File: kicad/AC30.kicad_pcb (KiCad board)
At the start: 2 copper layers, 173.5 x 122 mm, 119 parts, among them IC1 4013, IC10 555, IC11 4001, IC12 1489, IC13 4070, IC14 4053, IC15 1488, IC2 4001, IC3 4070, IC4 4558, IC5 4013, IC6 4053, IC7 4049, IC8 4013, IC9 4023, J1 Front panel harness 1, J12 Power input, J2 Front panel harness 2, J3 Computer interface (COMP), J4 Control interface, J5 Terminal interface (TERM), Q1 2N5210, Q10 2N5087, Q11 2N5087, Q2 2N5210, Q3 2N5087, Q4 2N5210, Q5 2N5210, Q6 2N5210, Q7 2N5210, Q8 2N5210, Q9 2N5087

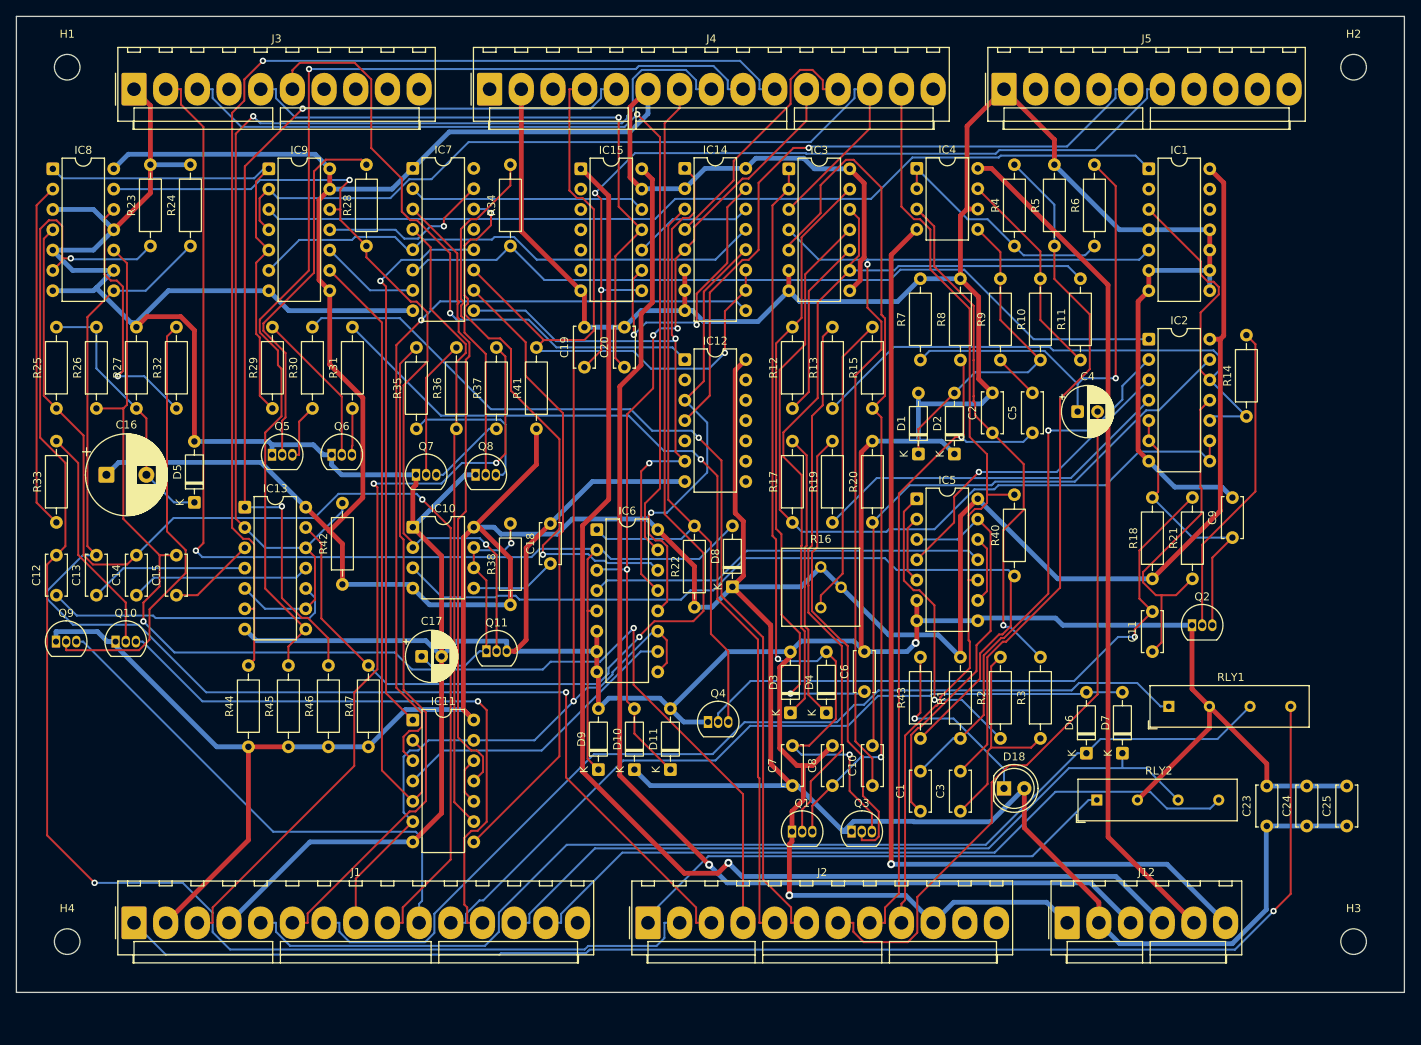
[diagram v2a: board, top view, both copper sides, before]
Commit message: Through-hole board: front-panel jumper pads in place of J1/J2
Both boards now wire the front panel to five rows of 0.1 in through-hole
pads with net names on the silkscreen (J1 SWITCHES, J2 LEDS, J13 MOTOR,
J14 MIC, J15 EAR) instead of the artwork's J1/J2 KK-396 headers.

The through-hole build weights board height at 60 (AC30_HEIGHT_W) so the
bottom row doesn't stretch the board; it is now 173.0 x 126.5 mm, fully
routed, ERC/DRC/parity clean. SMT board unchanged apart from symbol IDs
and the schematic note. AC30-settings.md updated.

Co-Authored-By: Claude Opus 5.5 <noreply@anthropic.com>
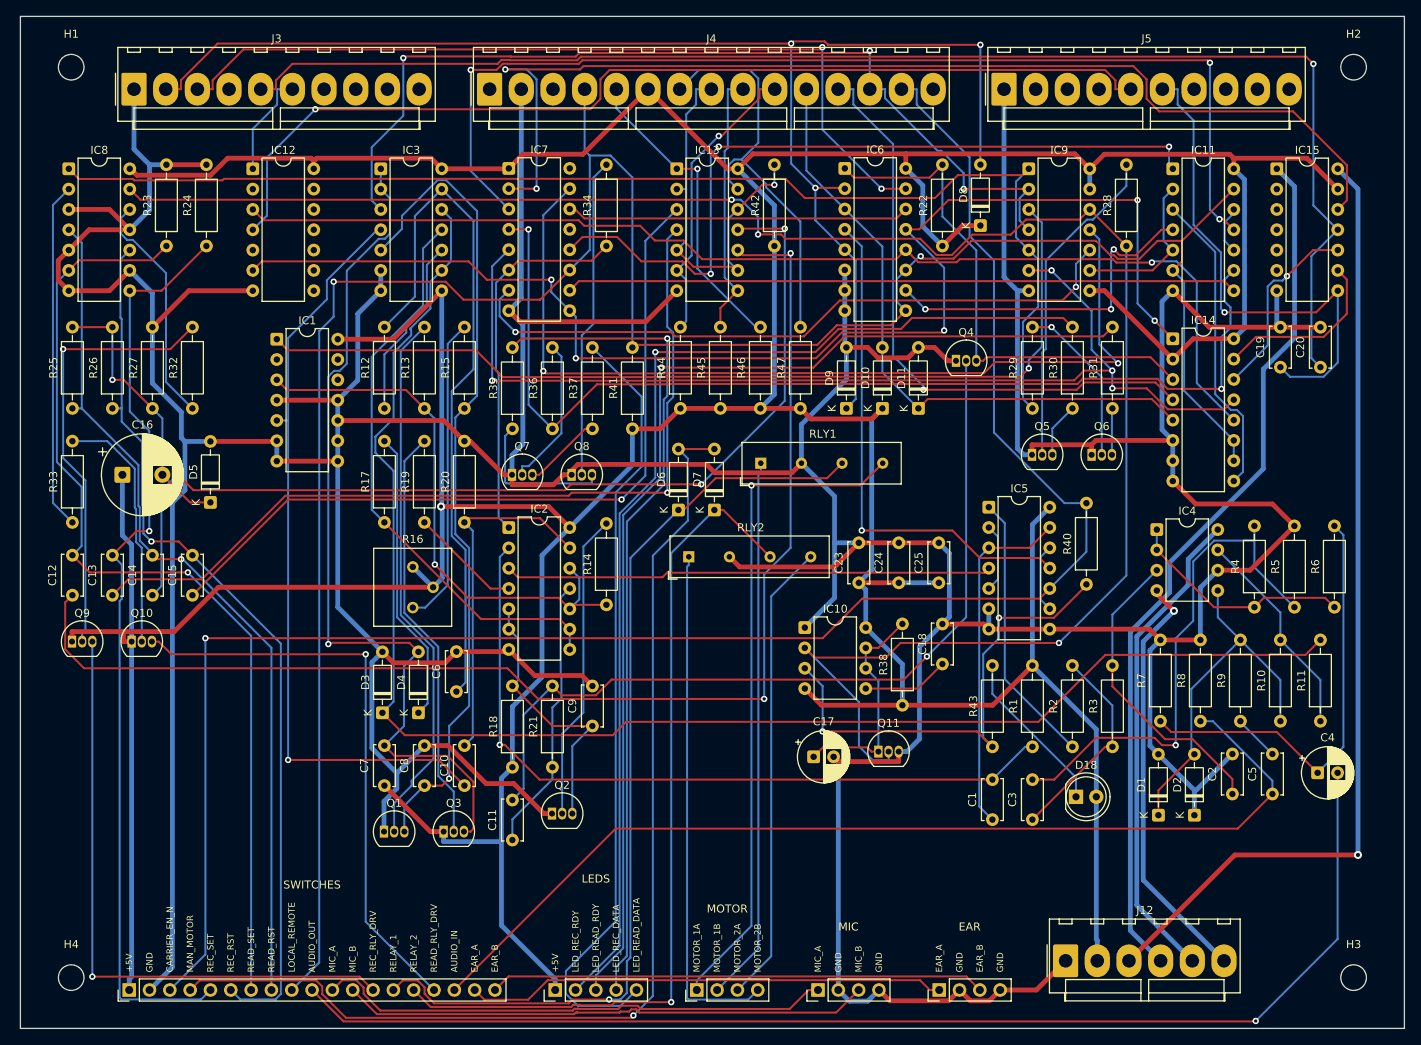
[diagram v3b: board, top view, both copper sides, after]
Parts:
- added J13: MOTOR, Connector_PinHeader_2.54mm:PinHeader_1x04_P2.54mm_Vertical, F.Cu at (114.5, 151.2)
- added J14: MIC, Connector_PinHeader_2.54mm:PinHeader_1x04_P2.54mm_Vertical, F.Cu at (129.7, 151.2)
- added J15: EAR, Connector_PinHeader_2.54mm:PinHeader_1x04_P2.54mm_Vertical, F.Cu at (144.8, 151.2)
- J1: value Front panel harness 1 -> SWITCHES; footprint Connector_Molex:Molex_KK-396_A-41791-0015_1x15_P3.96mm_Vertical -> Connector_PinHeader_2.54mm:PinHeader_1x19_P2.54mm_Vertical
- J2: value Front panel harness 2 -> LEDS; footprint Connector_Molex:Molex_KK-396_A-41791-0012_1x12_P3.96mm_Vertical -> Connector_PinHeader_2.54mm:PinHeader_1x05_P2.54mm_Vertical
- moved IC11 117.4 mm to (174.1, 48.5)
- moved IC1 111.1 mm to (62.0, 69.8)
- moved IC9 95.0 mm to (156.1, 48.5)
- moved Q6 95.0 mm to (163.9, 84.3)
- moved R28 95.0 mm to (168.2, 58.2)
- moved R29 95.0 mm to (156.5, 78.5)
- moved R30 95.0 mm to (161.5, 78.5)
- moved R31 95.0 mm to (166.5, 78.5)
- moved Q5 95.0 mm to (156.4, 84.3)
- moved IC15 87.0 mm to (187.1, 48.5)
- moved C19 87.0 mm to (187.5, 73.3)
- moved C20 87.0 mm to (192.5, 73.3)
- moved IC2 83.4 mm to (91.0, 93.4)
- moved C9 83.4 mm to (101.5, 118.2)
- moved R14 83.4 mm to (103.2, 103.0)
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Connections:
- J1 pad 1: /MOTOR_1A -> +5V
- J1 pad 10: /REC_RLY_DRV -> AUDIO_OUT
- J1 pad 11: /MAN_MOTOR -> /MIC_A
- J1 pad 12: /READ_RLY_DRV -> /MIC_B
- J1 pad 13: /RELAY_2 -> /REC_RLY_DRV
- J1 pad 14: /MOTOR_2A -> /RELAY_1
- J1 pad 15: unconnected-(J1-Pin_15-Pad15) -> /RELAY_2
- J1 pad 2: +5V -> GND
- J1 pad 3: /LED_READ_DATA -> CARRIER_EN_N
- J1 pad 4: GND -> /MAN_MOTOR
- J1 pad 5: /RELAY_1 -> /REC_SET
- J1 pad 6: /LED_REC_DATA -> /REC_RST
- J1 pad 7: /MOTOR_1B -> /READ_SET
- J1 pad 8: /LOCAL_REMOTE -> /READ_RST
- J1 pad 9: /READ_RST -> /LOCAL_REMOTE
- J2 pad 1: /MOTOR_2B -> +5V
- J2 pad 2: /READ_SET -> /LED_REC_RDY
- J2 pad 3: /REC_SET -> /LED_READ_RDY
- J2 pad 4: /REC_RST -> /LED_REC_DATA
- J2 pad 5: /LED_READ_RDY -> /LED_READ_DATA
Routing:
- net /REC_EN: track 108.2 -> 240.3 mm, vias 2 -> 3
- net /START_READ_P: track 37.3 -> 161.1 mm, vias 0 -> 2
- net CARRIER_EN_N: track 118.8 -> 230.5 mm, vias 0 -> 1
- net /CPU_RX: track 29.7 -> 139.5 mm, vias 0 -> 2
- net /START_RECORD: track 146.3 -> 36.9 mm
- net /START_READ: track 138.3 -> 33.4 mm, vias 1 -> 0
- net /STOP_READ_P: track 22.6 -> 125.2 mm, vias 0 -> 3
- net /CTRL_INVERT: track 150.7 -> 49.8 mm
- net /READ_EN: track 60.8 -> 156.2 mm
- net /CPU_RS232_IN: track 81.1 -> 175.3 mm
- net /DATA_SEL_N: track 21.6 -> 115.0 mm, vias 1 -> 2
- net /Mod/Demod & power input/DEM_LIM: track 98.9 -> 192.3 mm
- net /LOCAL_REMOTE: track 204.9 -> 294.8 mm
- net /MOTOR_1A: track 172.8 -> 83.5 mm
- net /START_REC_P: track 20.0 -> 108.6 mm, vias 0 -> 1
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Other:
- board size 173.5 x 122 mm -> 173 x 126.5 mm
- board text added: "+5V"
- board text added: "AUDIO_IN"
- board text added: "AUDIO_OUT"
- board text added: "CARRIER_EN_N"
- board text added: "EAR_A"
- board text added: "EAR_B"
- board text added: "GND"
- board text added: "LED_READ_DATA"
- board text added: "LED_READ_RDY"
- board text added: "LED_REC_DATA"
- board text added: "LED_REC_RDY"
- board text added: "LOCAL_REMOTE"
- board text added: "MAN_MOTOR"
- board text added: "MIC_A"
- board text added: "MIC_B"
- board text added: "MOTOR_1A"
- board text added: "MOTOR_1B"
- board text added: "MOTOR_2A"
- board text added: "MOTOR_2B"
- board text added: "READ_RLY_DRV"
- board text added: "READ_RST"
- board text added: "READ_SET"
- board text added: "REC_RLY_DRV"
- board text added: "REC_RST"
- board text added: "REC_SET"
- board text added: "RELAY_1"
- board text added: "RELAY_2"
